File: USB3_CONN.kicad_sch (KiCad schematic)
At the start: 4 parts, among them J3 USB3_A, U3 TPS2560

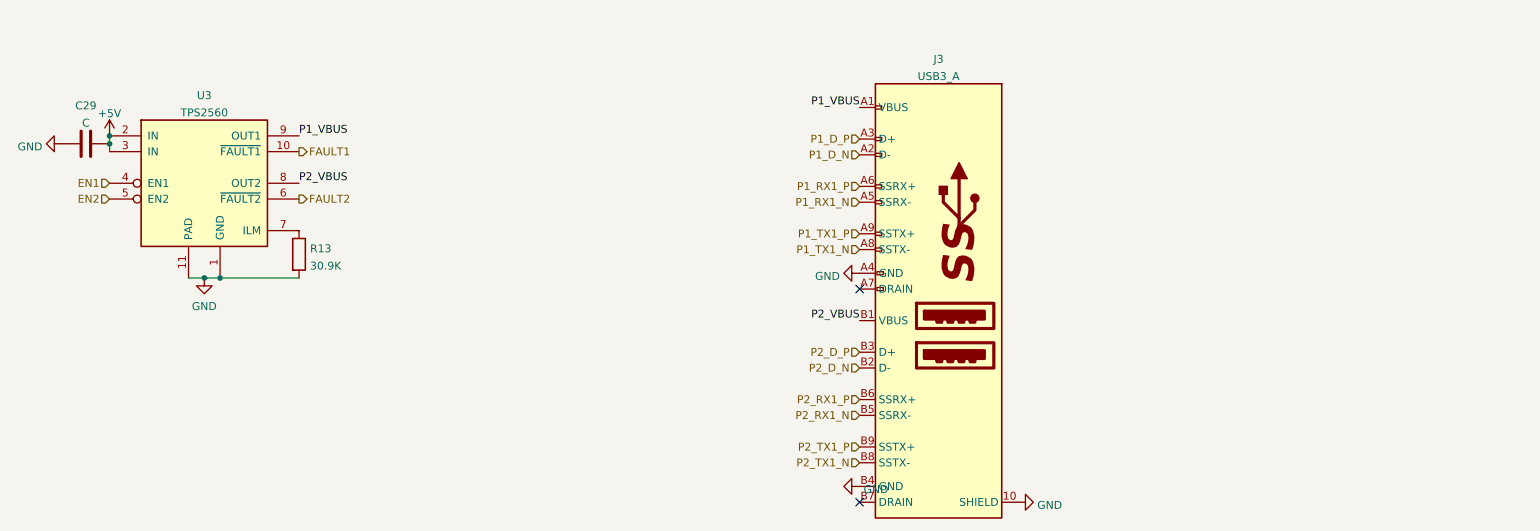
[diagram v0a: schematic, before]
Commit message: Initial layout and all parts added. Some pins still not connected to power
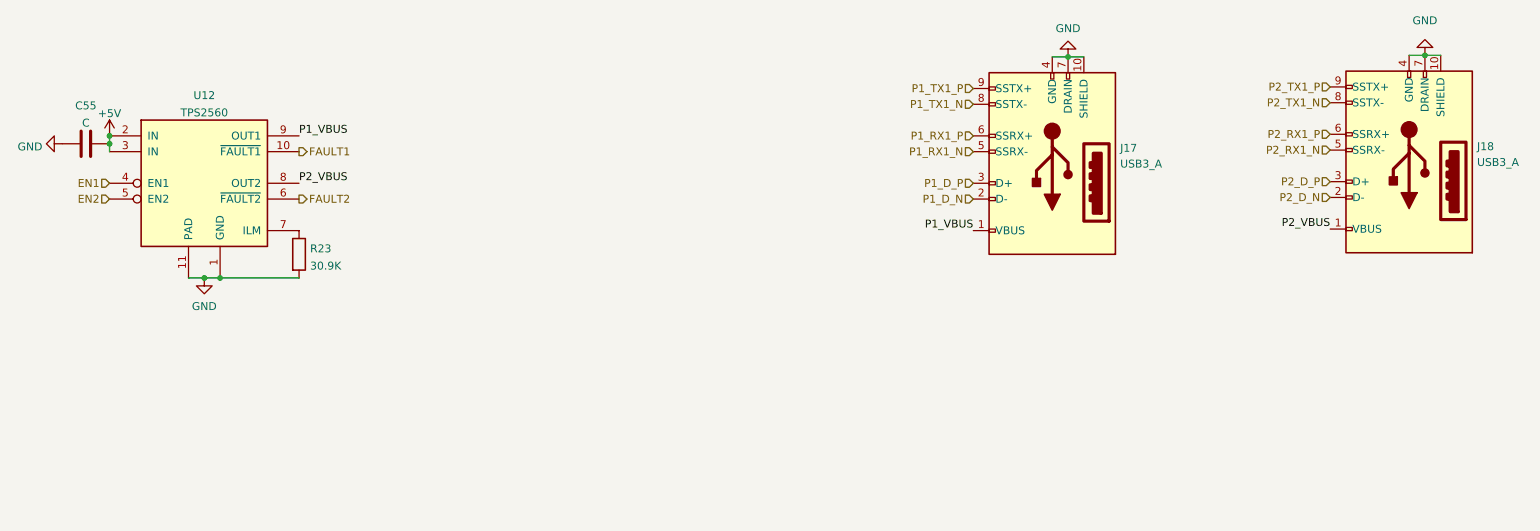
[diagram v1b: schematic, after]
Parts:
- removed J3: USB3_A, symbol CM4IO:USB3_A
- added J17, J18: USB3_A, Connector_USB:USB3_A_Molex_48393-001, symbol Connector:USB3_A
- renumbered C29 to C55, R13 to R23, U3 to U12
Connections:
- net GND: now also J17.10 (SHIELD), J17.4 (GND), J17.7 (DRAIN), J18.10 (SHIELD), J18.4 (GND), J18.7 (DRAIN)
- net P1_D_N: now also J17.2 (D-)
- net P1_D_P: now also J17.3 (D+)
- net P1_RX1_N: now also J17.5 (SSRX-)
- net P1_RX1_P: now also J17.6 (SSRX+)
- net P1_TX1_N: now also J17.8 (SSTX-)
- net P1_TX1_P: now also J17.9 (SSTX+)
- net P1_VBUS: now also J17.1 (VBUS)
- net P2_D_N: now also J18.2 (D-)
- net P2_D_P: now also J18.3 (D+)
- net P2_RX1_N: now also J18.5 (SSRX-)
- net P2_RX1_P: now also J18.6 (SSRX+)
- net P2_TX1_N: now also J18.8 (SSTX-)
- net P2_TX1_P: now also J18.9 (SSTX+)
- net P2_VBUS: now also J18.1 (VBUS)
- no-connect marks 2 -> 0

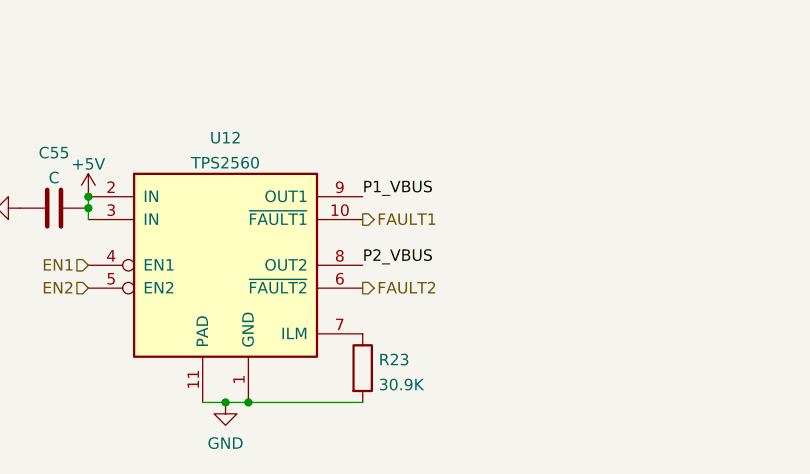
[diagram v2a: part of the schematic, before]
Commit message: mostly routed, need to add more layers fo power and finish low speed signal routing
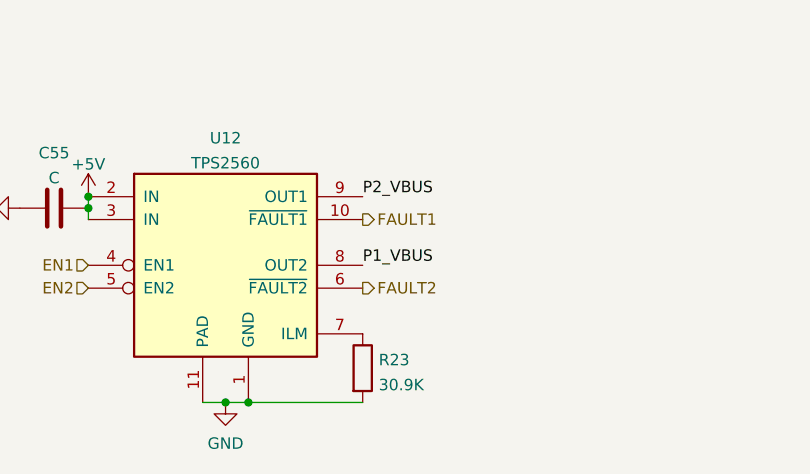
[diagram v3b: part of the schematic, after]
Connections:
- net P1_VBUS: now also U12.8 (OUT2); no longer U12.9 (OUT1)
- net P2_VBUS: now also U12.9 (OUT1); no longer U12.8 (OUT2)
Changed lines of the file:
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@@
 (kicad_sch (version 20210621) (generator eeschema)
   (paper "A4")
+  (junction (at 44.45 74.422) (diameter 0) (color 0 0 0 0))
+  (junction (at 59.69 97.282) (diameter 0) (color 0 0 0 0))
   (junction (at 44.45 75.692) (diameter 0) (color 0 0 0 0))
   (junction (at 198.628 61.722) (diameter 0) (color 0 0 0 0))
-  (junction (at 59.69 97.282) (diameter 0) (color 0 0 0 0))
+  (junction (at 62.23 97.282) (diameter 0) (color 0 0 0 0))
   (junction (at 256.032 61.468) (diameter 0) (color 0 0 0 0))
-  (junction (at 62.23 97.282) (diameter 0) (color 0 0 0 0))
-  (junction (at 44.45 74.422) (diameter 0) (color 0 0 0 0))
   (wire (pts (xy 44.45 75.692) (xy 44.45 76.962))
     (stroke (width 0) (type default) (color 0 0 0 0))
@@
     (effects (font (size 1.27 1.27)) (justify right bottom))
   )
-  (label "P1_VBUS" (at 74.93 74.422 0)
+  (label "P1_VBUS" (at 74.93 82.042 0)
     (effects (font (size 1.27 1.27)) (justify left bottom))
   )
-  (label "P2_VBUS" (at 74.93 82.042 0)
+  (label "P2_VBUS" (at 74.93 74.422 0)
     (effects (font (size 1.27 1.27)) (justify left bottom))
   )

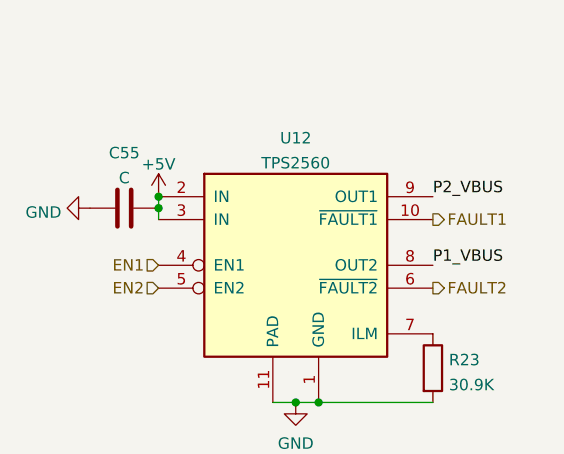
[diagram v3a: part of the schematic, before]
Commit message: Added usb to ethernet and changed mcu to stm32g4
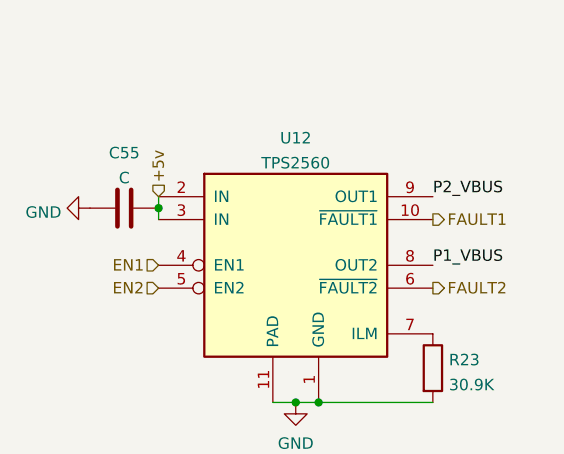
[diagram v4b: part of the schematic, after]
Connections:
- net +5V renamed +5v
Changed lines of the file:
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@@
 (kicad_sch (version 20210621) (generator eeschema)
   (paper "A4")
-  (junction (at 44.45 74.422) (diameter 0) (color 0 0 0 0))
-  (junction (at 59.69 97.282) (diameter 0) (color 0 0 0 0))
-  (junction (at 44.45 75.692) (diameter 0) (color 0 0 0 0))
-  (junction (at 198.628 61.722) (diameter 0) (color 0 0 0 0))
   (junction (at 62.23 97.282) (diameter 0) (color 0 0 0 0))
   (junction (at 256.032 61.468) (diameter 0) (color 0 0 0 0))
+  (junction (at 44.45 75.692) (diameter 0) (color 0 0 0 0))
+  (junction (at 59.69 97.282) (diameter 0) (color 0 0 0 0))
+  (junction (at 198.628 61.722) (diameter 0) (color 0 0 0 0))
   (wire (pts (xy 44.45 75.692) (xy 44.45 76.962))
     (stroke (width 0) (type default) (color 0 0 0 0))
@@
     (effects (font (size 1.27 1.27)) (justify right))
   )
+  (hierarchical_label "+5v" (shape input) (at 44.45 74.422 90)
+    (effects (font (size 1.27 1.27)) (justify left))
+  )
   (hierarchical_label "P1_RX1_N" (shape input) (at 183.388 76.962 180)
     (effects (font (size 1.27 1.27)) (justify right))
@@
       (effects (font (size 1.27 1.27)) hide)
     )
-    (pin "1")
-  )
-  (symbol (lib_id "power:+5V") (at 44.45 74.422 0) (unit 1)
-    (in_bom yes) (on_board yes) (fields_autoplaced)
-    (property "Reference" "#PWR068" (id 0) (at 44.45 78.232 0)
-      (effects (font (size 1.27 1.27)) hide)
-    )
-    (property "Value" "+5V" (id 1) (at 44.45 70.8175 0))
-    (property "Footprint" "" (id 2) (at 44.45 74.422 0)
-      (effects (font (size 1.27 1.27)) hide)
-    )
-    (property "Datasheet" "" (id 3) (at 44.45 74.422 0)
-      (effects (font (size 1.27 1.27)) hide)
-    )
